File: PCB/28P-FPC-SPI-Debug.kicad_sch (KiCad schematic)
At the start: 20 parts, among them J1 Conn_01x24, J3 SFV24R-1STBE1HLF, Q1 Si1308EDL

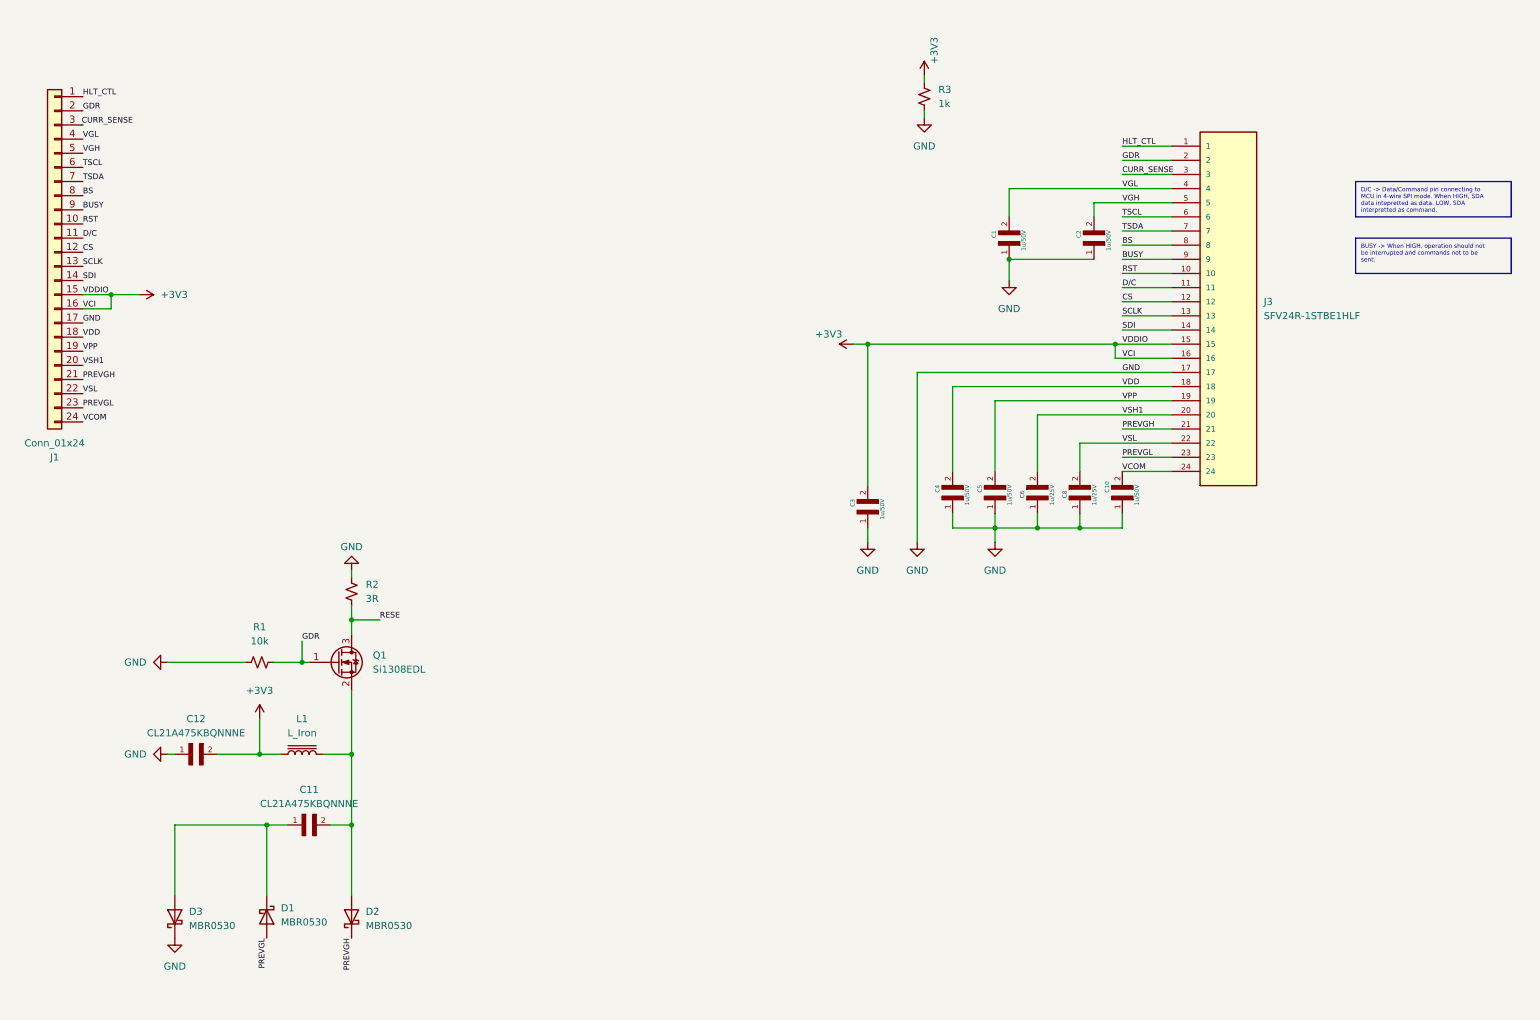
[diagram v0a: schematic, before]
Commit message: Modified power switch circuit and added note. Added note for boost converter.
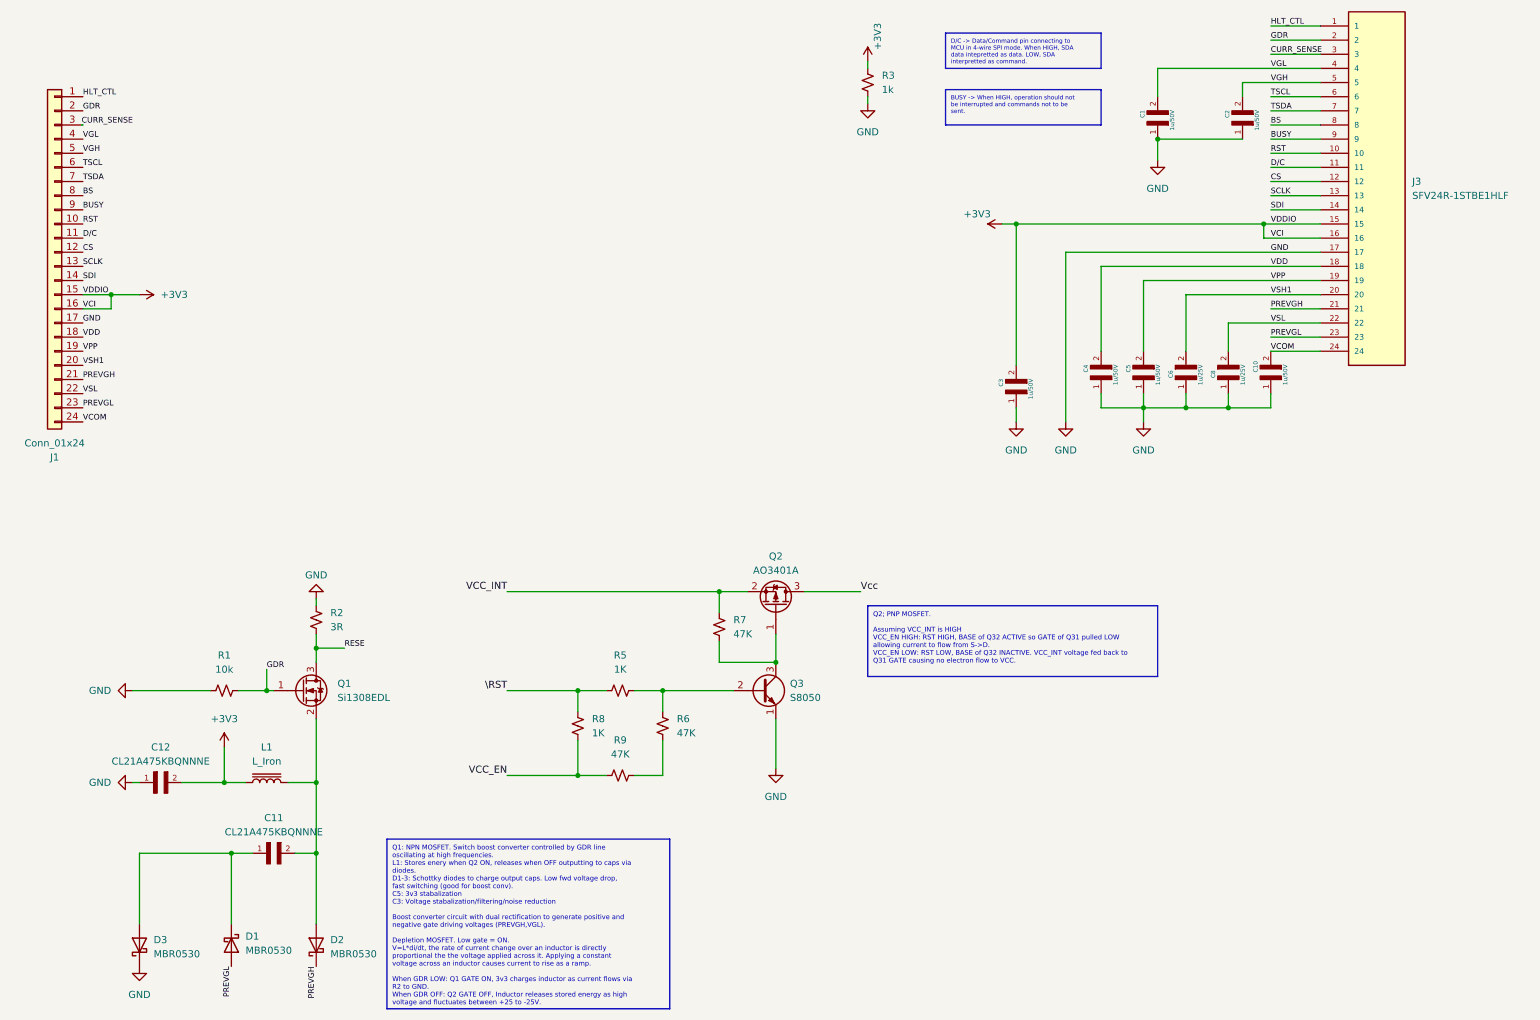
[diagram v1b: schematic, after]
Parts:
- added Q2: AO3401A, Package_TO_SOT_SMD:SOT-23, symbol Transistor_FET:AO3401A
- added Q3: S8050, Package_TO_SOT_THT:TO-92_Inline, symbol Transistor_BJT:S8050
- added R5, R8: 1K, Resistor_SMD:R_0201_0603Metric, symbol Device:R_Small_US
- added R6, R7, R9: 47K, Resistor_SMD:R_0201_0603Metric, symbol Device:R_Small_US
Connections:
- net GND: now also Q3.1 (E)
- new net: Q2.1 (G), Q3.3 (C), R7.1
- new net: R6.1, R9.1
- new net: Q3.2 (B), R5.1, R6.2
- new net VCC_EN: R8.2, R9.2
- new net VCC_INT: Q2.2 (S), R7.2
- new net Vcc: Q2.3 (D)
- new net \RST: R5.2, R8.1
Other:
- moved on the sheet: C1, C10, C11, C12, C2, C3, C4, C5, C6, C8, D1, D2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

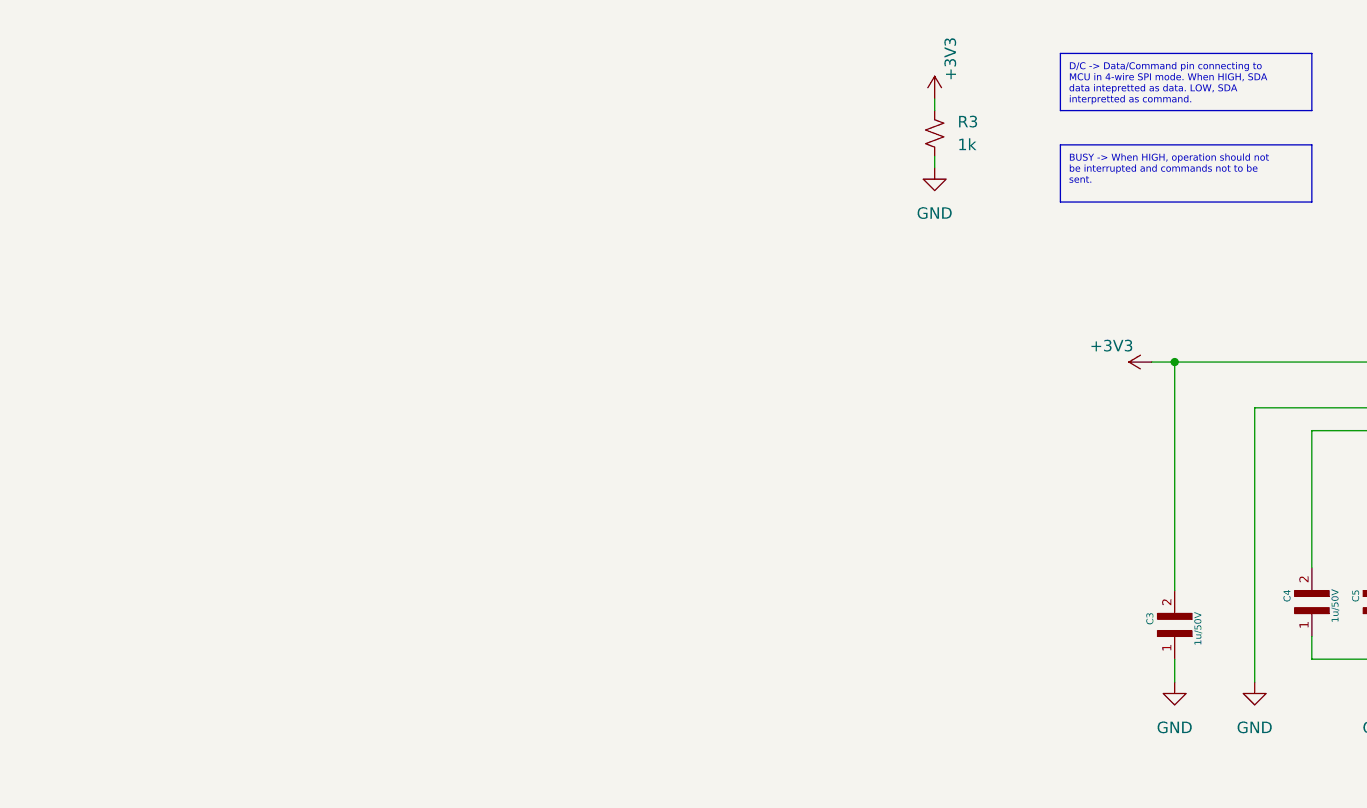
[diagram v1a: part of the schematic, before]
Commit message: Modified power enable circuit to v2.2 ref design and added note.
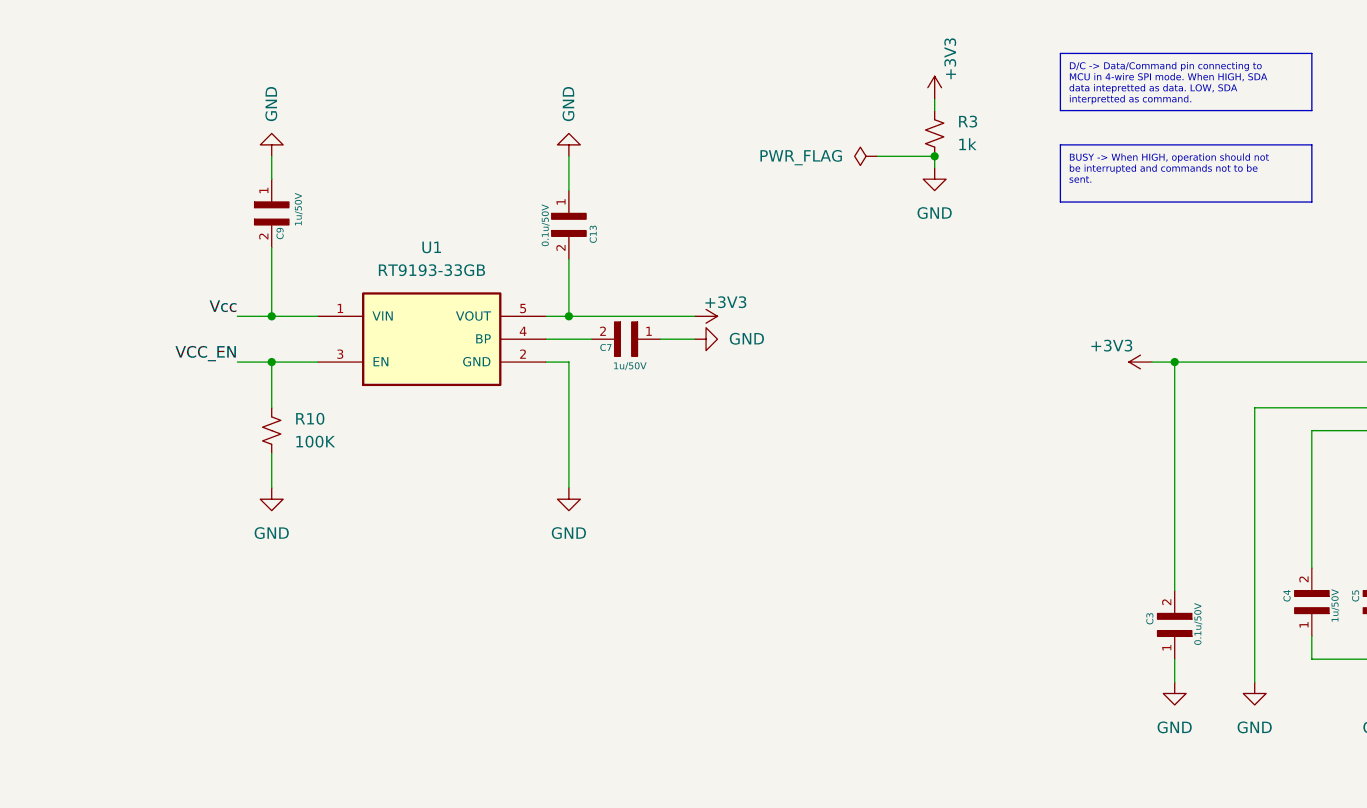
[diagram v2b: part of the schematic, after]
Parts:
- added C13: 0.1u/50V, capacitors-cam:CAPC2012X140N, symbol Capacitors:MBASU168AB5105KTNA01
- added C7, C9: 1u/50V, capacitors-cam:CAPC2012X140N, symbol Capacitors:MBASU168AB5105KTNA01
- added R10: 100K, Resistor_SMD:R_0201_0603Metric, symbol Device:R_Small_US
- added U1: RT9193-33GB, VoltageRegulators:SOT94P279X129-5N, symbol VoltageRegulators:RT9193-33GB
- C3: value 1u/50V -> 0.1u/50V
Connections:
- net +3V3: now also C13.2, U1.5 (VOUT)
- net GND: now also C13.1, C7.1, C9.1, R10.1, U1.2 (GND)
- net VCC_EN: now also R10.2, U1.3 (EN)
- net Vcc: now also C9.2, U1.1 (VIN)
- new net: C7.2, U1.4 (BP)

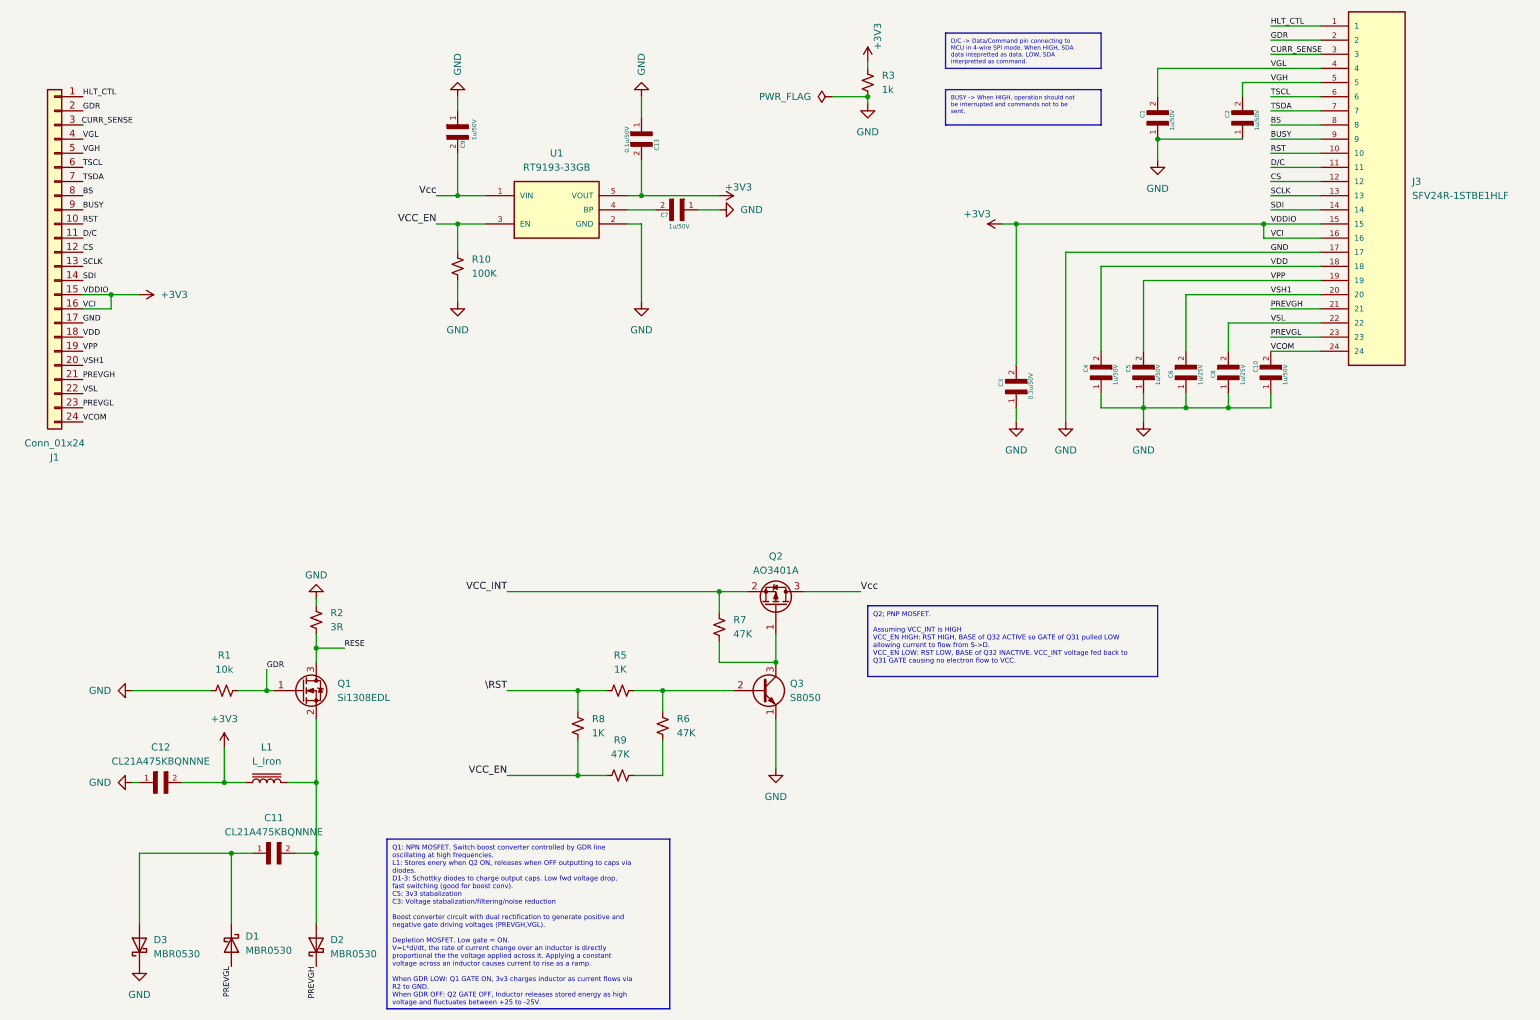
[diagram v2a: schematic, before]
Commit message: Added voltage level shifter TXB018PW
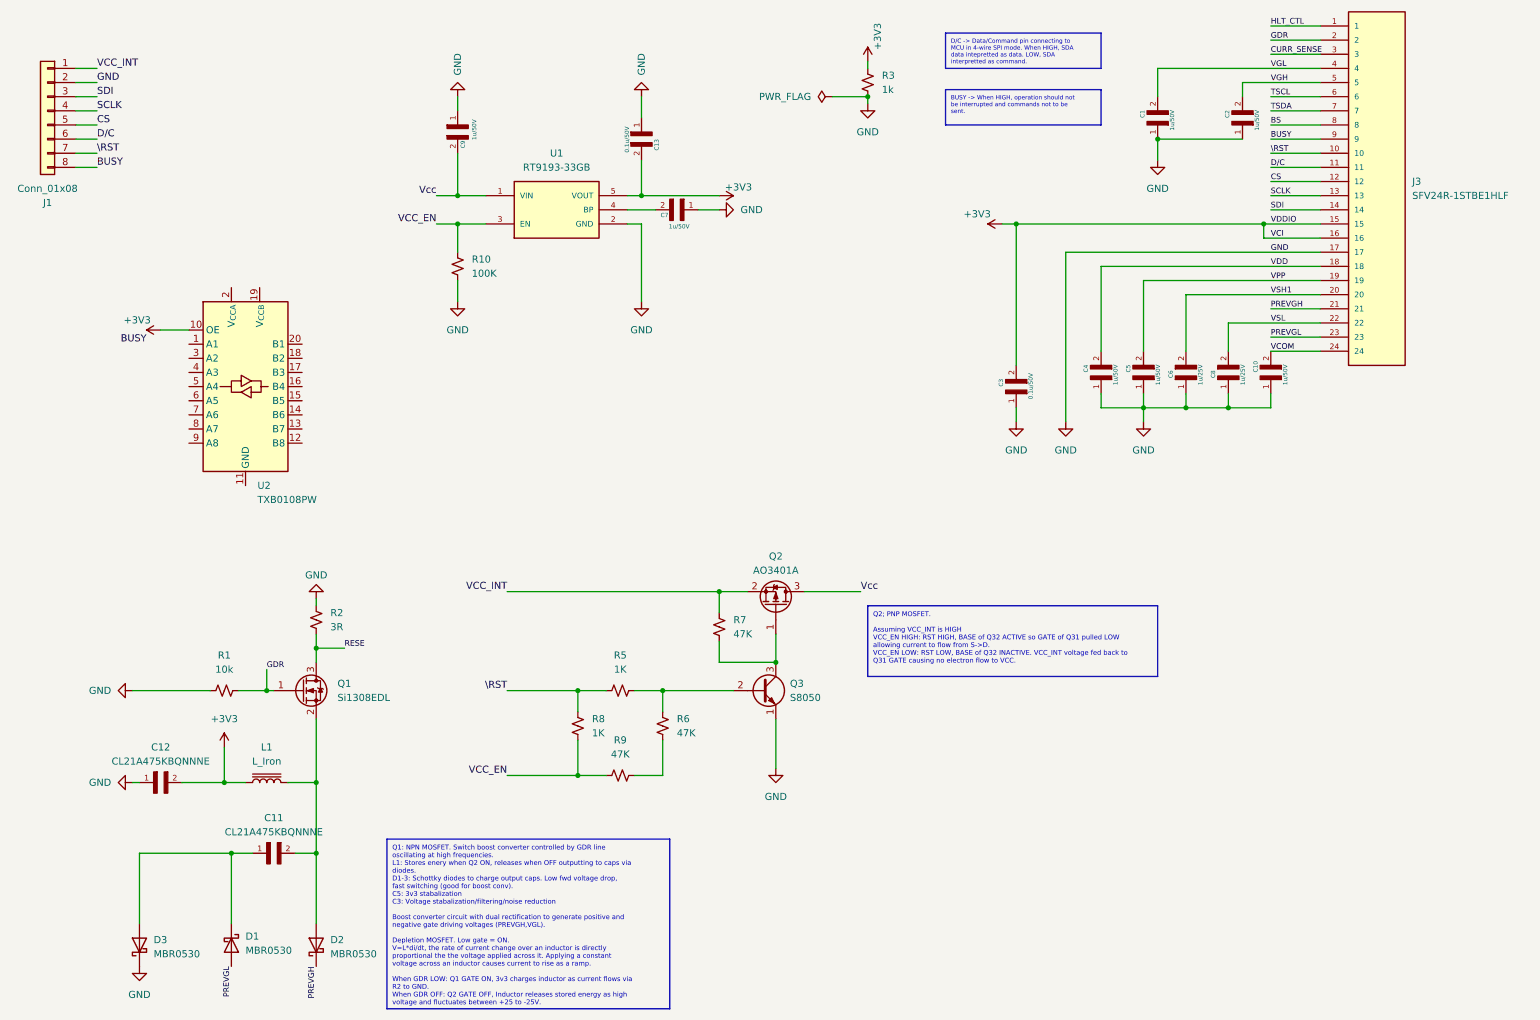
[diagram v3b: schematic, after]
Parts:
- removed J1: Conn_01x24, Connector_PinHeader_2.54mm:PinHeader_2x12_P2.54mm_Vertical, symbol Connector_Generic:Conn_01x24
- added J1: Conn_01x08, Connector_Samtec_HLE_THT:Samtec_HLE-104-02-xx-DV-TE_2x04_P2.54mm_Horizontal, symbol Connector_Generic:Conn_01x08
- added U2: TXB0108PW, Package_SO:TSSOP-20_4.4x6.5mm_P0.65mm, symbol Logic_LevelTranslator:TXB0108PW
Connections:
- net RST is gone; now on net \RST: J3.10
- net +3V3: now also U2.10 (OE)
- net BUSY: now also J1.8 (Pin_8)
- net CS: now also J1.5 (Pin_5)
- net D/C: now also J1.6 (Pin_6)
- net GND: now also R10.2, J1.2 (Pin_2); no longer R10.1
- net SCLK: now also J1.4 (Pin_4)
- net SDI: now also J1.3 (Pin_3)
- net VCC_EN: now also R10.1; no longer R10.2
- net VCC_INT: now also J1.1 (Pin_1)
- net \RST: now also J1.7 (Pin_7)
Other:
- moved on the sheet: R10
